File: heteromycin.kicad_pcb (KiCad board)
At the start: 4 copper layers, 200 x 100 mm, 376 parts, among them J1 920-0135-01, J10 Micro_SD_Card_Det_Hirose_DM3AT, J11 20021121-00010C4LF, J12 70543-0001, J13 70543-0001, J14 70543-0001, J15 70543-0001, J16 70543-0001, J17 70543-0001, J18 70543-0001, J19 70543-0001, J2 4DB-P108-06, J20 70543-0003, J21 70543-0002, J22 70543-0002, J23 70543-0002, J24 Conn_02x20_Odd_Even, J3 39531-1002, J4 39531-1002, J5 70543-0003, J6 70543-0003, J7 70543-0003, J8 70543-0003, J9 70543-0003, Q1 DMMT5401, Q10 PMPB11EN, Q11 PSMN1R2-30YLC,115, Q12 PSMN1R2-30YLC,115, Q13 PSMN1R2-30YLC,115, Q14 PMPB11EN, Q15 PMPB11EN, Q16 PMPB11EN, Q17 PMPB11EN, Q18 PMPB11EN, Q19 PMPB11EN, Q2 DMG2305UX, Q20 PMPB11EN, Q21 PMPB11EN, Q22 PMPB11EN, Q23 PMPB11EN, Q24 PMPB11EN, Q25 PMPB11EN, Q26 PMPB11EN, Q27 PMPB11EN, Q28 PMPB11EN, Q29 PMPB11EN, Q3 PMPB11EN, Q30 PMPB11EN, Q31 PMPB11EN, Q32 PMPB11EN, Q33 PMPB11EN, Q34 PMPB11EN, Q35 PMPB11EN, Q36 PMPB11EN, Q37 PMPB11EN, Q38 PMPB11EN, Q39 PMPB11EN, Q4 PMPB11EN, Q40 PMPB11EN, Q41 PMPB11EN, Q42 PMPB11EN, Q43 PMPB11EN, Q44 PMPB11EN, Q45 PMPB11EN, Q46 PMPB11EN, Q47 PMPB11EN, Q48 PMPB11EN, Q49 PMPB11EN, Q5 PMPB11EN, Q6 PMPB11EN, Q7 PMPB11EN, Q8 PMPB11EN, Q9 PMPB11EN, SW1 PTS645VL39-2, U1 CAT24C32, U10 TMC2160-TA, U2 i3A, U3 AP2112K-3.3TRG1, U4 CAT24C32, U5 STM32F765VIT6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

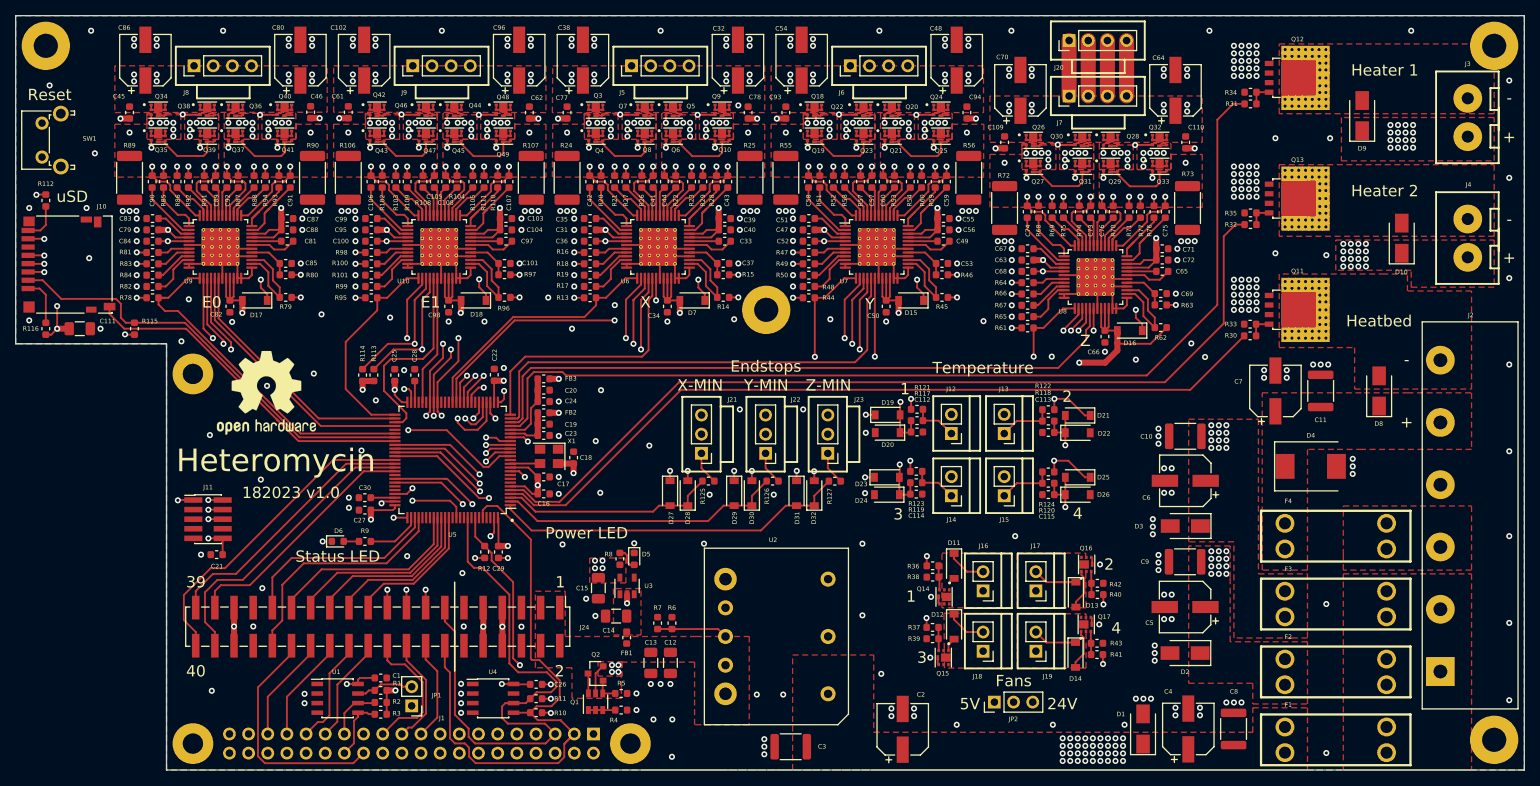
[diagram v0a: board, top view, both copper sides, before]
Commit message: Add transistor for boot selection
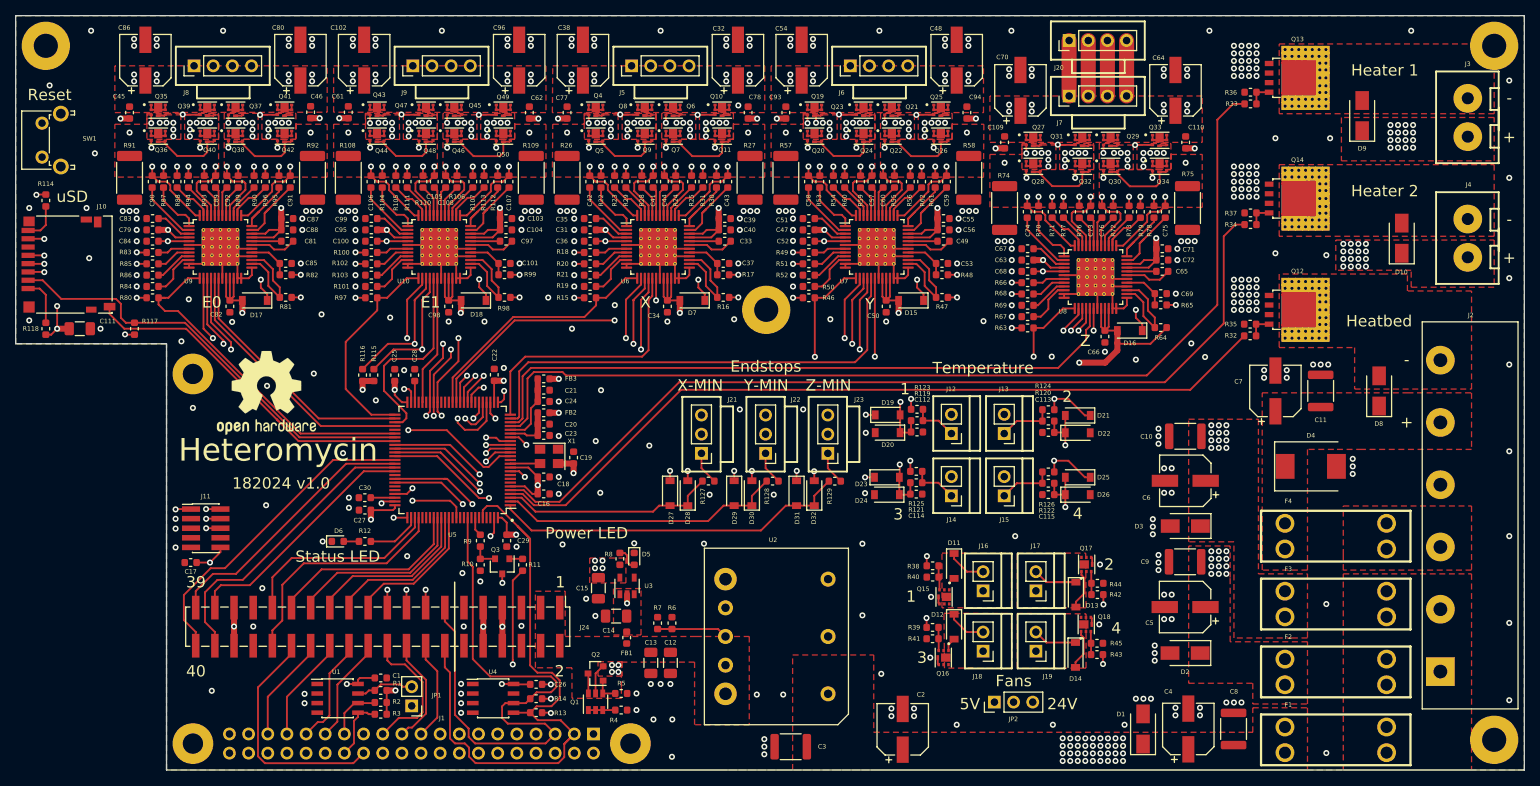
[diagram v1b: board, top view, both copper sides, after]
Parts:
- added Q3: MMBT3904-7-F, Package_TO_SOT_SMD:SOT-23, F.Cu at (109.5, 123.0)
- added R11: 10k, Resistor_SMD:R_0603_1608Metric, F.Cu at (112.2, 122.8)
- added R9: 10k, Resistor_SMD:R_0603_1608Metric, F.Cu at (106.6, 119.6)
- R10: renamed from R12; value 47k -> 10k
- moved C17 3.61 mm to (68.2, 122.5)
- moved C29 1.86 mm to (110.1, 119.6)
- moved R10 1.79 mm to (106.6, 122.8), turned to 90 degrees
- moved J11 1.24 mm to (70.2, 118.0)
- renumbered C21 to C17, C17 to C18, C18 to C19, C19 to C20, C20 to C21, Q9 to Q10, Q10 to Q11, Q11 to Q12, Q12 to Q13, Q13 to Q14, Q14 to Q15, Q15 to Q16, Q16 to Q17, Q17 to Q18, Q18 to Q19, Q19 to Q20, Q20 to Q21, Q21 to Q22, Q22 to Q23, Q23 to Q24, Q24 to Q25, Q25 to Q26, Q26 to Q27, Q27 to Q28, Q28 to Q29, Q29 to Q30, Q30 to Q31, Q31 to Q32, Q32 to Q33, Q33 to Q34, Q34 to Q35, Q35 to Q36, Q36 to Q37, Q37 to Q38, Q38 to Q39, Q3 to Q4, Q39 to Q40, Q40 to Q41, Q41 to Q42, Q42 to Q43, Q43 to Q44, Q44 to Q45, Q45 to Q46, Q46 to Q47, Q47 to Q48, Q48 to Q49, Q4 to Q5, Q49 to Q50, Q5 to Q6, Q6 to Q7, Q7 to Q8, Q8 to Q9, R98 to R100, R99 to R101, R100 to R102, R101 to R103, R102 to R104, R103 to R105, R104 to R106, R105 to R107, R106 to R108, R107 to R109, R108 to R110, R109 to R111, R110 to R112, R111 to R113, R112 to R114, R113 to R115, R114 to R116, R115 to R117, R116 to R118, R117 to R119, R9 to R12, R118 to R120, R119 to R121, R120 to R122, R121 to R123, R122 to R124, R123 to R125, R124 to R126, R125 to R127, R126 to R128, R127 to R129, R10 to R13, R11 to R14, R13 to R15, R14 to R16, R15 to R17, R16 to R18, R17 to R19, R18 to R20, R19 to R21, R20 to R22, R21 to R23, R22 to R24, R23 to R25, R24 to R26, R25 to R27, R26 to R28, R27 to R29, R28 to R30, R29 to R31, R30 to R32, R31 to R33, R32 to R34, R33 to R35, R34 to R36, R35 to R37, R36 to R38, R37 to R39, R38 to R40, R39 to R41, R40 to R42, R41 to R43, R42 to R44, R43 to R45, R44 to R46, R45 to R47, R46 to R48, R47 to R49, R48 to R50, R49 to R51, R50 to R52, R51 to R53, R52 to R54, R53 to R55, R54 to R56, R55 to R57, R56 to R58, R57 to R59, R58 to R60, R59 to R61, R60 to R62, R61 to R63, R62 to R64, R63 to R65, R64 to R66, R65 to R67, R66 to R68, R67 to R69, R68 to R70, R69 to R71, R70 to R72, R71 to R73, R72 to R74, R73 to R75, R74 to R76, R75 to R77, R76 to R78, R77 to R79, R78 to R80, R79 to R81, R80 to R82, R81 to R83, R82 to R84, R83 to R85, R84 to R86, R85 to R87, R86 to R88, R87 to R89, R88 to R90, R89 to R91, R90 to R92, R91 to R93, R92 to R94, R93 to R95, R94 to R96, R95 to R97, R96 to R98, R97 to R99
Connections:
- R10 pad 1: /MCU/BOOT -> GND
- R10 pad 2: GND -> Net-(Q3-Pad2)
- U5 pad 94: /MCU/BOOT -> /MCU/BOOTpin
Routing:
- net /Connectors/nRESET: track 194.5 -> 212.5 mm
- net /MCU/BOOT: track 32.0 -> 23.4 mm
- net Net-(Q3-Pad2): track 0.00 -> 3.58 mm
- net /Connectors/SDA: track 82.2 -> 84.8 mm
- net GND: track 164.9 -> 162.3 mm, vias 354 -> 356
- net /MCU/BOOTpin: track 0.00 -> 2.54 mm
- net /Connectors/SCL: track 78.7 -> 80.6 mm
- net Net-(Q3-Pad1): track 0.00 -> 1.76 mm
- net /Connectors/SWDIO: track 32.3 -> 33.1 mm
- net VDD3V3: track 199.9 -> 200.4 mm, vias 50 -> 51
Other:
- board text added: "182024 v1.0"
- board text removed: "182023 v1.0"

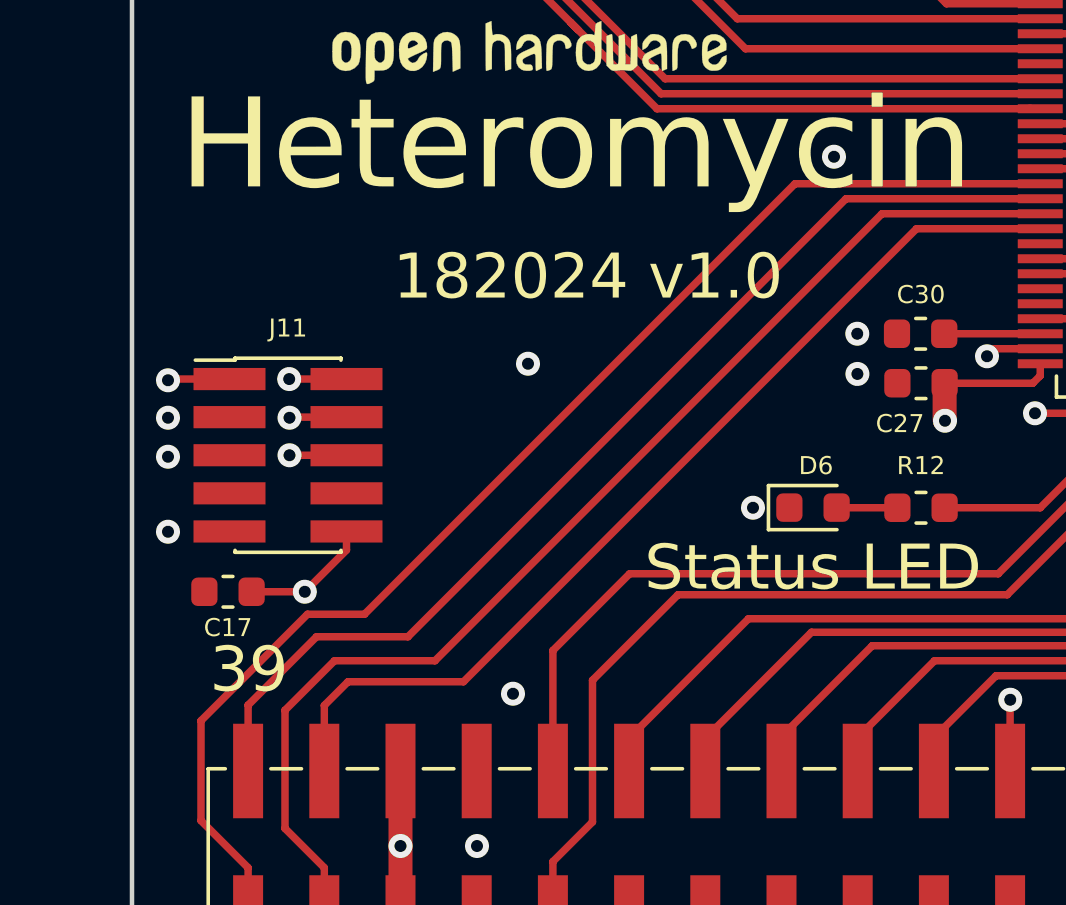
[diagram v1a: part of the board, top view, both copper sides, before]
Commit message: Move the nRESET cap a little bit
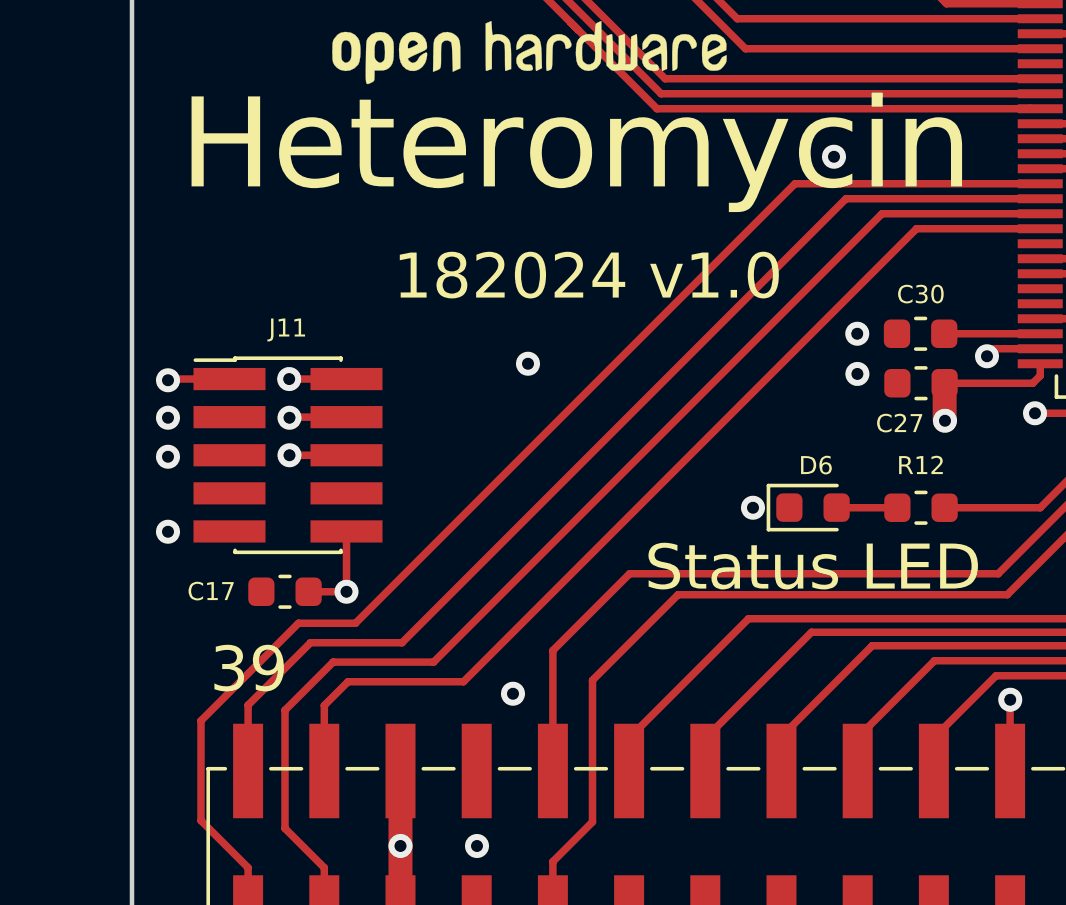
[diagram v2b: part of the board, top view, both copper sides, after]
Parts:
- moved C17 1.90 mm to (70.1, 122.5)
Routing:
- net /Connectors/nRESET: track 212.5 -> 211.3 mm
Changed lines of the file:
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@@
     (thickness 1.6)
     (drawings 72)
-    (tracks 4295)
+    (tracks 4292)
     (zones 0)
     (modules 379)
@@
   )
   (module Capacitor_SMD:C_0603_1608Metric (layer F.Cu)
-    (at 68.2 122.5)
+    (at 70.1 122.5)
     (descr "Capacitor SMD 0603 (1608 Metric), square (rectangular) end terminal, IPC_7351 nominal, (Body size source: http://www.tortai-tech.com/upload/download/2011102023233369053.pdf), generated with kicad-footprint-generator")
     (tags capacitor)
     (attr smd)
-    (fp_text reference C17 (at 0 1.2) (layer F.SilkS)
+    (fp_text reference C17 (at -2.45 0) (layer F.SilkS)
       (effects (font (size 0.6 0.6) (thickness 0.1)))
     )
@@
   (segment (start 94.624999 116.074999) (end 70.875001 116.074999) (width 0.25) (layer In2.Cu) (net 68))
   (segment (start 95.1 116.55) (end 94.624999 116.074999) (width 0.25) (layer In2.Cu) (net 68))
-  (via (at 70.25 117.95) (size 0.8) (drill 0.4) (layers F.Cu B.Cu) (net 69))
-  (segment (start 72.15 117.95) (end 70.25 117.95) (width 0.25) (layer F.Cu) (net 69) (status 10))
   (via (at 97.6 114.3) (size 0.8) (drill 0.4) (layers F.Cu B.Cu) (net 69))
   (segment (start 102.6 114.3) (end 97.6 114.3) (width 0.25) (layer F.Cu) (net 69))
   (segment (start 103.425 116.55) (end 103.425 115.125) (width 0.25) (layer F.Cu) (net 69) (status 10))
   (segment (start 103.425 115.125) (end 102.6 114.3) (width 0.25) (layer F.Cu) (net 69))
+  (via (at 70.25 117.95) (size 0.8) (drill 0.4) (layers F.Cu B.Cu) (net 69))
+  (segment (start 72.15 117.95) (end 70.25 117.95) (width 0.25) (layer F.Cu) (net 69) (status 10))
   (segment (start 97.6 114.865685) (end 97.6 114.3) (width 0.25) (layer In2.Cu) (net 69))
-  (segment (start 97.6 115.123002) (end 97.6 114.865685) (width 0.25) (layer In2.Cu) (net 69))
   (segment (start 94.773002 117.95) (end 97.6 115.123002) (width 0.25) (layer In2.Cu) (net 69))
+  (segment (start 97.6 115.123002) (end 97.6 114.865685) (width 0.25) (layer In2.Cu) (net 69))
   (segment (start 70.25 117.95) (end 94.773002 117.95) (width 0.25) (layer In2.Cu) (net 69))
   (segment (start 72.1375 120.5025) (end 72.15 120.49) (width 0.25) (layer F.Cu) (net 70) (status 30))
@@
   (segment (start 82.7 104.95) (end 97.05 104.95) (width 0.25) (layer In2.Cu) (net 70))
   (segment (start 82.25 104.95) (end 82.7 104.95) (width 0.25) (layer In2.Cu) (net 70))
-  (segment (start 72.15 121.11) (end 72.15 120.49) (width 0.25) (layer F.Cu) (net 70))
-  (segment (start 70.76 122.5) (end 70.76 122.5) (width 0.25) (layer F.Cu) (net 70))
-  (segment (start 68.9875 122.5) (end 70.76 122.5) (width 0.25) (layer F.Cu) (net 70))
-  (segment (start 70.76 122.5) (end 72.15 121.11) (width 0.25) (layer F.Cu) (net 70))
-  (via (at 70.76 122.5) (size 0.8) (drill 0.4) (layers F.Cu B.Cu) (net 70))
-  (segment (start 69.514999 119.314999) (end 70.76 120.56) (width 0.25) (layer In2.Cu) (net 70))
-  (segment (start 69.514999 109.085001) (end 69.514999 119.314999) (width 0.25) (layer In2.Cu) (net 70))
-  (segment (start 70.76 120.56) (end 70.76 122.5) (width 0.25) (layer In2.Cu) (net 70))
-  (segment (start 73.65 104.95) (end 69.514999 109.085001) (width 0.25) (layer In2.Cu) (net 70))
-  (segment (start 77.2 104.95) (end 73.65 104.95) (width 0.25) (layer In2.Cu) (net 70))
   (segment (start 97.05 104.95) (end 77.2 104.95) (width 0.25) (layer In2.Cu) (net 70))
   (segment (start 77.2 101.3) (end 77.2 104.95) (width 0.25) (layer In2.Cu) (net 70))
@@
   (segment (start 48.9 76.6) (end 47.05 78.45) (width 0.25) (layer In2.Cu) (net 70))
   (segment (start 47.05 78.45) (end 47.05 86.976998) (width 0.25) (layer In2.Cu) (net 70))
-  (segment (start 69.5 122.5) (end 70.76 122.5) (width 0.25) (layer In2.Cu) (net 70))
   (segment (start 107.54 149.1) (end 72.75 149.1) (width 0.25) (layer In2.Cu) (net 70))
   (segment (start 108.9 147.74) (end 107.54 149.1) (width 0.25) (layer In2.Cu) (net 70))
@@
   (segment (start 66.8 139.4) (end 66.8 125.2) (width 0.25) (layer In2.Cu) (net 70))
   (segment (start 72 144.6) (end 66.8 139.4) (width 0.25) (layer In2.Cu) (net 70))
+  (via (at 72.15 122.5) (size 0.8) (drill 0.4) (layers F.Cu B.Cu) (net 70))
+  (segment (start 72.15 120.49) (end 72.15 122.5) (width 0.25) (layer F.Cu) (net 70))
+  (segment (start 70.8875 122.5) (end 72.15 122.5) (width 0.25) (layer F.Cu) (net 70))
+  (segment (start 69.5 122.5) (end 72.15 122.5) (width 0.25) (layer In2.Cu) (net 70))
+  (segment (start 69.514999 112.635001) (end 77.2 104.95) (width 0.25) (layer In2.Cu) (net 70))
+  (segment (start 69.514999 118.564999) (end 69.514999 112.635001) (width 0.25) (layer In2.Cu) (net 70))
+  (segment (start 72.15 122.5) (end 72.15 121.2) (width 0.25) (layer In2.Cu) (net 70))
+  (segment (start 72.15 121.2) (end 69.514999 118.564999) (width 0.25) (layer In2.Cu) (net 70))
   (segment (start 97.925 98.4625) (end 97.9 98.4375) (width 0.25) (layer F.Cu) (net 71) (status 30))
   (segment (start 97.925 101.25) (end 97.925 98.4625) (width 0.25) (layer F.Cu) (net 71) (status 30))
@@
   (segment (start 108.6 103.4) (end 102.65 109.35) (width 0.25) (layer In2.Cu) (net 284))
   (segment (start 99.35 146.45) (end 94.95 146.45) (width 0.25) (layer In2.Cu) (net 284))
-  (segment (start 68.87 131.7) (end 68.87 133.525) (width 0.25) (layer F.Cu) (net 285) (status 20))
-  (segment (start 87.1 108.9) (end 72.75 123.25) (width 0.25) (layer F.Cu) (net 285))
-  (segment (start 95.275 108.9) (end 87.1 108.9) (width 0.25) (layer F.Cu) (net 285) (status 10))
-  (segment (start 70.85 123.25) (end 67.3 126.8) (width 0.25) (layer F.Cu) (net 285))
-  (segment (start 72.75 123.25) (end 70.85 123.25) (width 0.25) (layer F.Cu) (net 285))
-  (segment (start 67.3 130.13) (end 68.87 131.7) (width 0.25) (layer F.Cu) (net 285))
+  (segment (start 68.87 131.7) (end 68.87 133.525) (width 0.25) (layer F.Cu) (net 285))
+  (segment (start 87.1 108.9) (end 72.45 123.55) (width 0.25) (layer F.Cu) (net 285))
+  (segment (start 95.275 108.9) (end 87.1 108.9) (width 0.25) (layer F.Cu) (net 285))
+  (segment (start 70.55 123.55) (end 67.3 126.8) (width 0.25) (layer F.Cu) (net 285))
+  (segment (start 72.45 123.55) (end 70.55 123.55) (width 0.25) (layer F.Cu) (net 285))
   (segment (start 67.3 126.8) (end 67.3 130.13) (width 0.25) (layer F.Cu) (net 285))
+  (segment (start 67.3 130.13) (end 68.87 131.7) (width 0.25) (layer F.Cu) (net 285))
   (segment (start 68.87 128.475) (end 68.87 127.4) (width 0.25) (layer F.Cu) (net 286) (status 30))
-  (segment (start 74.2 124) (end 88.8 109.4) (width 0.25) (layer F.Cu) (net 286))
-  (segment (start 88.8 109.4) (end 95.275 109.4) (width 0.25) (layer F.Cu) (net 286) (status 20))
-  (segment (start 68.87 128.475) (end 68.87 126.28) (width 0.25) (layer F.Cu) (net 286) (status 10))
-  (segment (start 71.15 124) (end 74.2 124) (width 0.25) (layer F.Cu) (net 286))
-  (segment (start 68.87 126.28) (end 71.15 124) (width 0.25) (layer F.Cu) (net 286))
-  (segment (start 71.41 131.7) (end 71.41 133.525) (width 0.25) (layer F.Cu) (net 287) (status 20))
-  (segment (start 90 109.9) (end 75.1 124.8) (width 0.25) (layer F.Cu) (net 287))
-  (segment (start 75.1 124.8) (end 71.75 124.8) (width 0.25) (layer F.Cu) (net 287))
-  (segment (start 95.275 109.9) (end 90 109.9) (width 0.25) (layer F.Cu) (net 287) (status 10))
-  (segment (start 71.75 124.8) (end 70.1 126.45) (width 0.25) (layer F.Cu) (net 287))
-  (segment (start 70.1 126.45) (end 70.1 130.39) (width 0.25) (layer F.Cu) (net 287))
+  (segment (start 74 124.2) (end 88.8 109.4) (width 0.25) (layer F.Cu) (net 286))
+  (segment (start 88.8 109.4) (end 95.275 109.4) (width 0.25) (layer F.Cu) (net 286))
+  (segment (start 70.95 124.2) (end 74 124.2) (width 0.25) (layer F.Cu) (net 286))
+  (segment (start 68.87 128.475) (end 68.87 126.28) (width 0.25) (layer F.Cu) (net 286))
+  (segment (start 68.87 126.28) (end 70.95 124.2) (width 0.25) (layer F.Cu) (net 286))
+  (segment (start 90 109.9) (end 75.055263 124.844737) (width 0.25) (layer F.Cu) (net 287))
+  (segment (start 95.275 109.9) (end 90 109.9) (width 0.25) (layer F.Cu) (net 287))
+  (segment (start 71.41 131.7) (end 71.41 133.525) (width 0.25) (layer F.Cu) (net 287))
   (segment (start 70.1 130.39) (end 71.41 131.7) (width 0.25) (layer F.Cu) (net 287))
+  (segment (start 75.055263 124.844737) (end 71.705263 124.844737) (width 0.25) (layer F.Cu) (net 287))
+  (segment (start 71.705263 124.844737) (end 70.1 126.45) (width 0.25) (layer F.Cu) (net 287))
+  (segment (start 70.1 126.45) (end 70.1 130.39) (width 0.25) (layer F.Cu) (net 287))
   (segment (start 91.15 110.4) (end 95.275 110.4) (width 0.25) (layer F.Cu) (net 288) (status 20))
   (segment (start 76.05 125.5) (end 91.15 110.4) (width 0.25) (layer F.Cu) (net 288))
@@
   (segment (start 112.1875 122) (end 112.2 122.0125) (width 0.25) (layer F.Cu) (net 335))
   (segment (start 110.45 122) (end 112.1875 122) (width 0.25) (layer F.Cu) (net 335))
-  (segment (start 88.492499 119.7) (end 88.4875 119.695001) (width 0.25) (layer F.Cu) (net 338) (status 30))
-  (segment (start 90.5125 119.7) (end 88.492499 119.7) (width 0.25) (layer F.Cu) (net 338) (status 30))
   (segment (start 106.6125 122) (end 106.6 122.0125) (width 0.25) (layer F.Cu) (net 336))
   (segment (start 108.55 122) (end 106.6125 122) (width 0.25) (layer F.Cu) (net 336))
@@
   (segment (start 105.925 118.1375) (end 106.6 118.8125) (width 0.25) (layer F.Cu) (net 337))
   (segment (start 105.925 116.55) (end 105.925 118.1375) (width 0.25) (layer F.Cu) (net 337))
+  (segment (start 88.492499 119.7) (end 88.4875 119.695001) (width 0.25) (layer F.Cu) (net 338) (status 30))
+  (segment (start 90.5125 119.7) (end 88.492499 119.7) (width 0.25) (layer F.Cu) (net 338) (status 30))
   (zone (net 208) (net_name "/Stepper Motor E1/BMB1") (layer In2.Cu) (hatch edge 0.508)
     (priority 1)

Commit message: Update TXCO and STM32CubeMX configuration file
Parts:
- X1: value ECS-TXO-3225-160-TR -> ECS-TXO-3225-200-TR
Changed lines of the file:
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@@
       (effects (font (size 0.6 0.6) (thickness 0.1)))
     )
-    (fp_text value ECS-TXO-3225-160-TR (at 0 2.55 180) (layer F.Fab)
+    (fp_text value ECS-TXO-3225-200-TR (at 0 2.55 180) (layer F.Fab)
       (effects (font (size 0.6 0.6) (thickness 0.1)))
     )

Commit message: Correct the name of the micro SD card reader
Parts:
- J10: value Micro_SD_Card_Det_Hirose_DM3AT -> DM3D-SF
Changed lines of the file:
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@@
       (effects (font (size 0.6 0.6) (thickness 0.1)))
     )
-    (fp_text value Micro_SD_Card_Det_Hirose_DM3AT (at 1.8 11.6 270) (layer F.Fab)
+    (fp_text value DM3D-SF (at 1.8 11.6 270) (layer F.Fab)
       (effects (font (size 0.6 0.6) (thickness 0.1)))
     )

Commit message: Change PI connector to a cheaper one
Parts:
- J1: value 920-0135-01 -> M20-7832046
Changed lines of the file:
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@@
       (effects (font (size 0.6 0.6) (thickness 0.1)))
     )
-    (fp_text value 920-0135-01 (at -1.27 -51.03 90) (layer B.Fab)
+    (fp_text value M20-7832046 (at -1.27 -51.03 90) (layer B.Fab)
       (effects (font (size 0.6 0.6) (thickness 0.1)) (justify mirror))
     )

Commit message: Increase date code for v1.0 release
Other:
- board text added: "182026 v1.0"
- board text removed: "182024 v1.0"
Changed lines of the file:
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@@
     (effects (font (size 1.5 1.5) (thickness 0.3)))
   )
-  (gr_text "182024 v1.0" (at 80.2 112) (layer F.SilkS)
+  (gr_text "182026 v1.0" (at 80.2 112) (layer F.SilkS)
     (effects (font (size 1.5 1.5) (thickness 0.3)))
   )
